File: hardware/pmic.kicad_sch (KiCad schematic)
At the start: 11 parts, among them U501 RK809-5

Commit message: Calculate captured PMIC capacitor bank bias margins
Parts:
- C501, C502, C503, C504, C505, C506, C507, C508: Qualification Effective-capacitance review and load stability pending -> Typical bias curve reviewed; combined-corner aging and loop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

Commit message: Capture PMIC 1.8V buck channel and expand connectivity checks
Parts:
- added C509, C510, C511, C512: 22uF / 25V, Capacitor_SMD:C_1210_3225Metric, symbol Device:C_Small
- added L505: 0.47uH, Inductor_SMD:L_Coilcraft_XxL4020, symbol Device:L_Small
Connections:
- net GND: now also C509.2, C510.2, C511.2, C512.2
- net PMIC_SW5: now reaches U501.53 (SW5)
- net PMIC_SW5: now also L505.1
- net 3V3_MAIN: now reaches U501.54 (VCC9)
- net 3V3_MAIN: now also C512.1
- net VCC_1V8: now reaches U501.59 (FB5)
- net VCC_1V8: now also C509.1, C510.1, C511.1, L505.2
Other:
- note added: "BUCK5: 1.8V startup / 2.5A rated; 3 x 22uF output bank"
- note added: "PMIC capture in progress — BUCK1 / BUCK2 / BUCK5"
- note removed: "PMIC capture in progress — BUCK1 / BUCK2"
- moved on the sheet: U501D

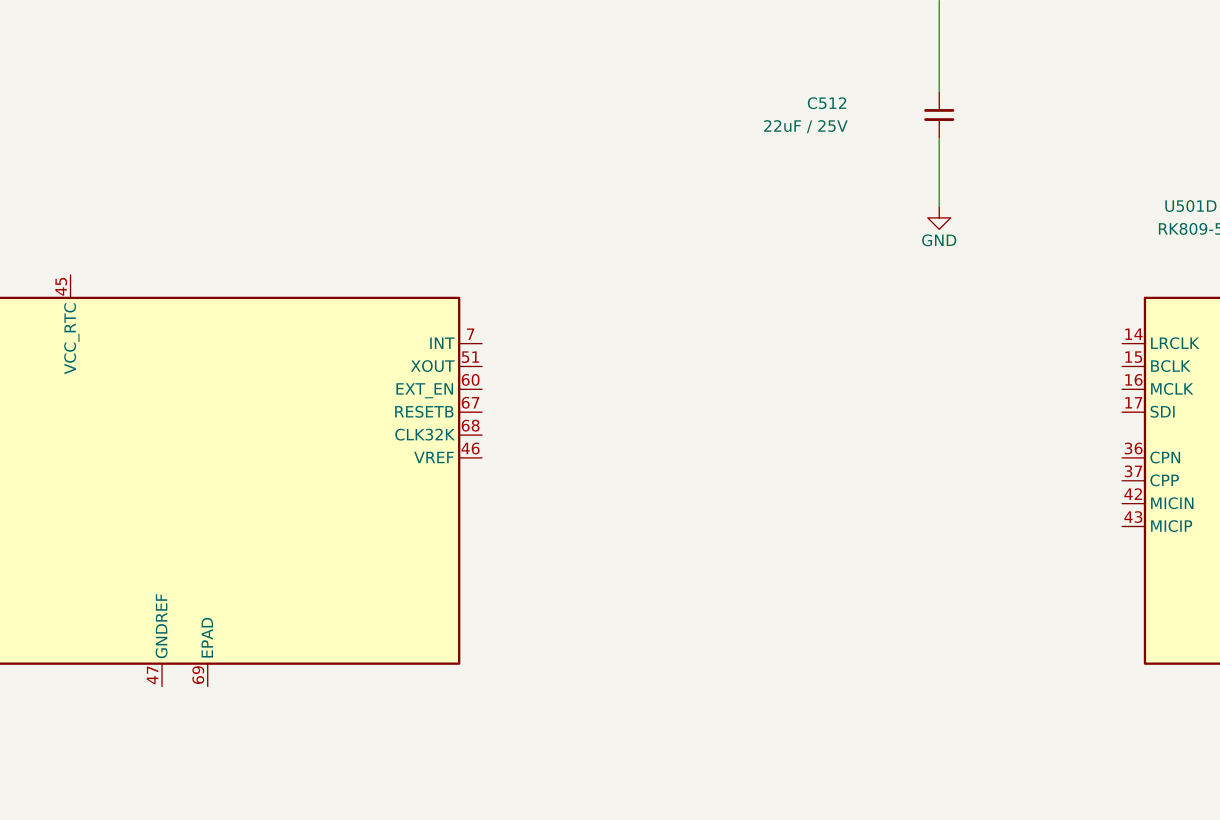
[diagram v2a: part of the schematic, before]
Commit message: Capture PMIC ground return and processor reset network
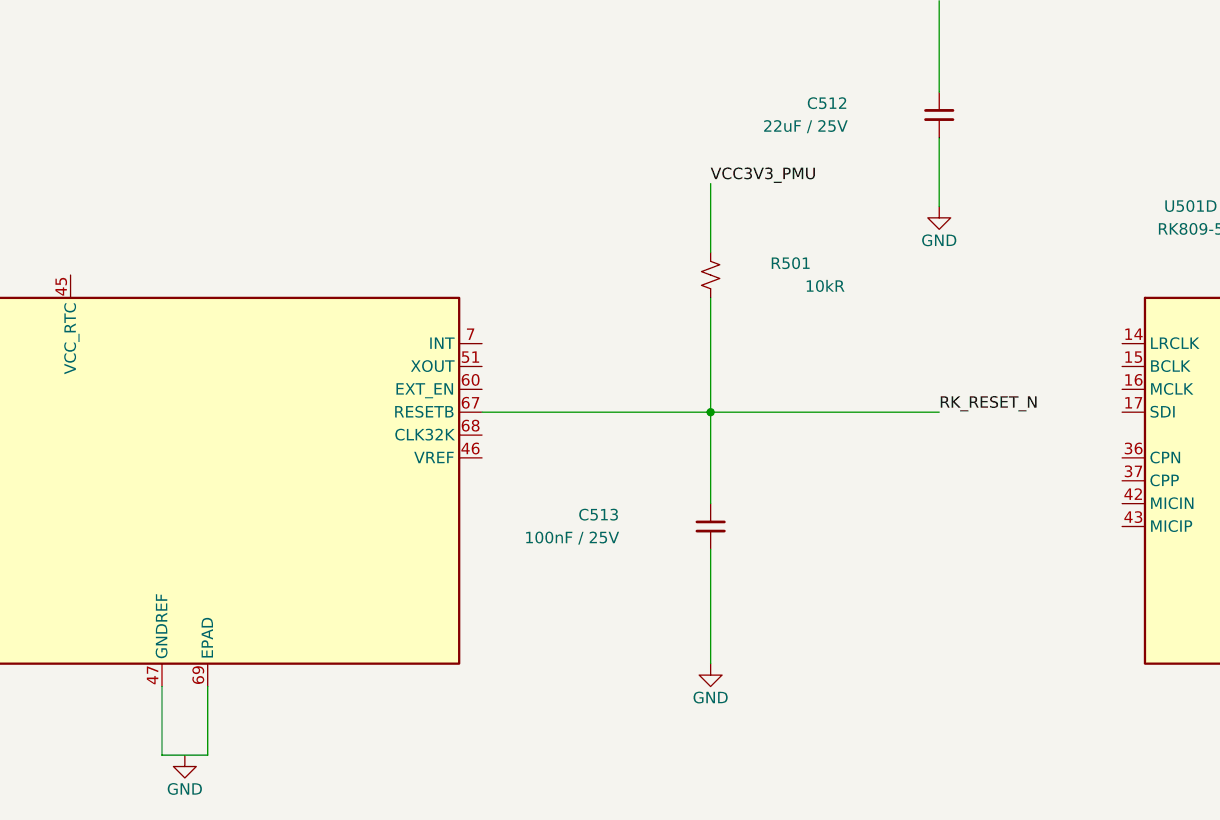
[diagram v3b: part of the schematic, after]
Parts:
- added C513: 100nF / 25V, Capacitor_SMD:C_0603_1608Metric, symbol Device:C_Small
- added R501: 10kR, Resistor_SMD:R_0603_1608Metric, symbol Device:R_Small_US
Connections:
- net GND: now also C513.2
- net at U501.47 (GNDREF): now also U501.69 (EPAD)
- net RK_RESET_N: now reaches U501.67 (RESETB)
- net RK_RESET_N: now also C513.1, R501.2
- new net VCC3V3_PMU: R501.1

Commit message: Capture PMIC RTC and internal-reference bypass circuits
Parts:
- added C514, C515: 1uF / 25V, Capacitor_SMD:C_0603_1608Metric, symbol Device:C_Small
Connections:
- net 3V3_MAIN: now also U501.45 (VCC_RTC), C514.1
- net GND: now also C514.2, C515.2
- net at U501.46 (VREF): now also C515.1

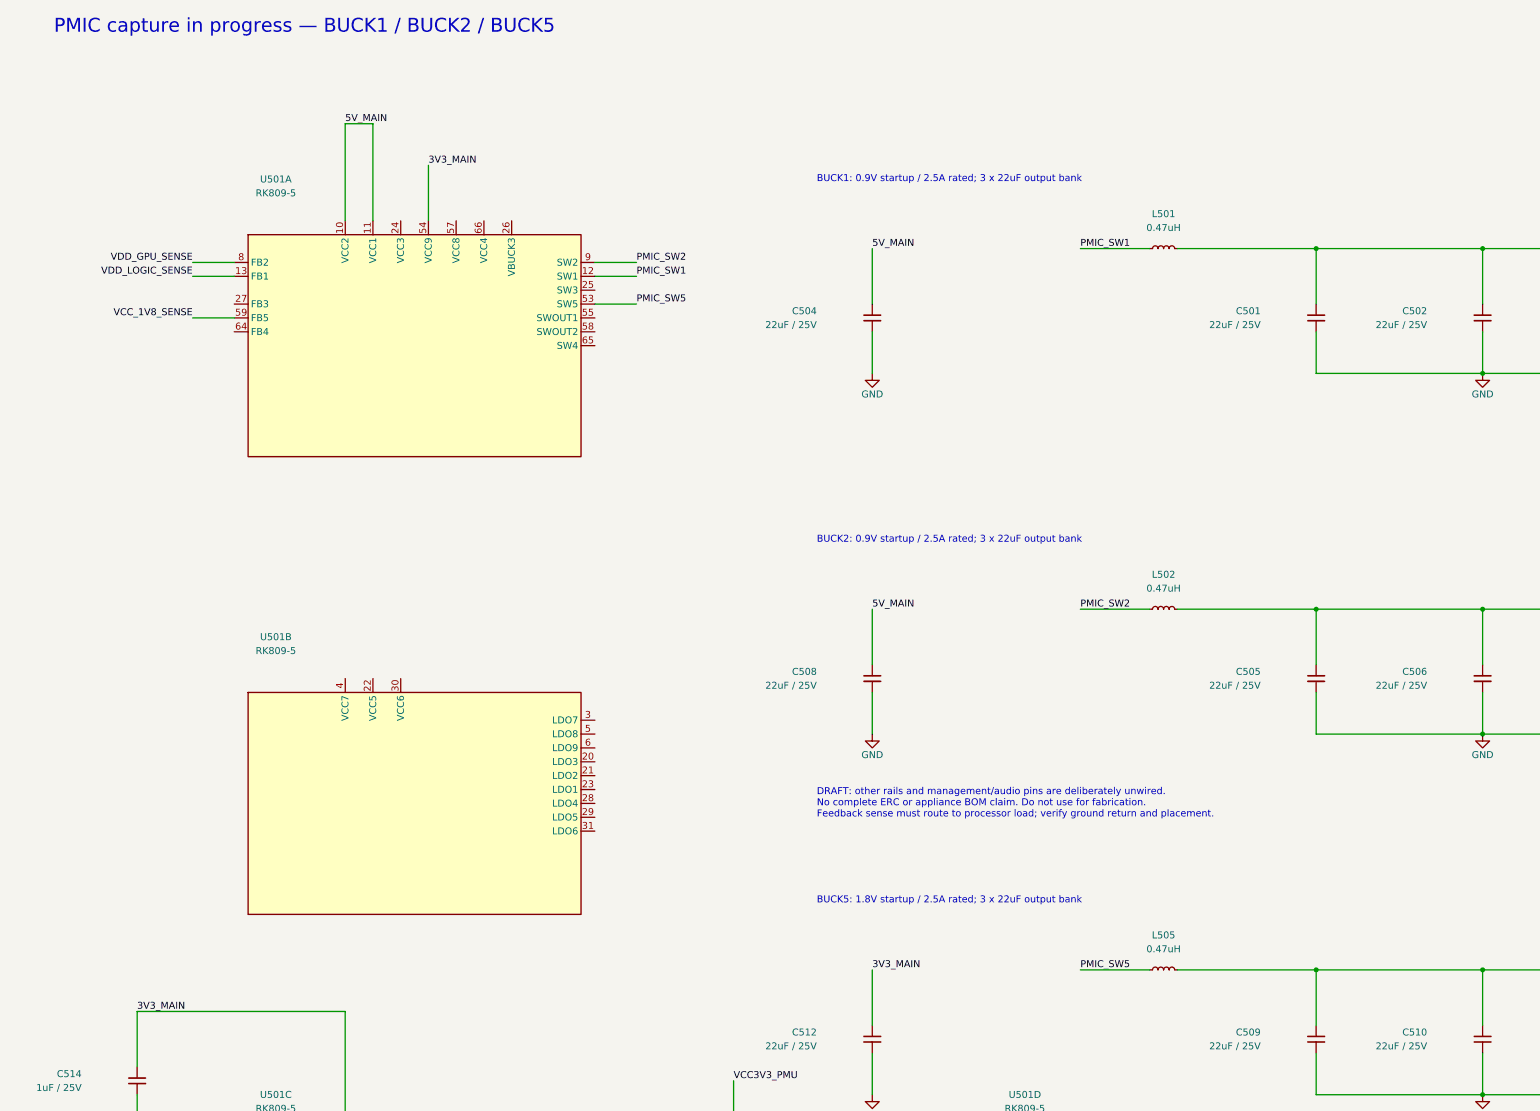
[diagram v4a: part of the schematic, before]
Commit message: Enforce PMIC RTC voltage rule and capture 3.3V PMU LDO
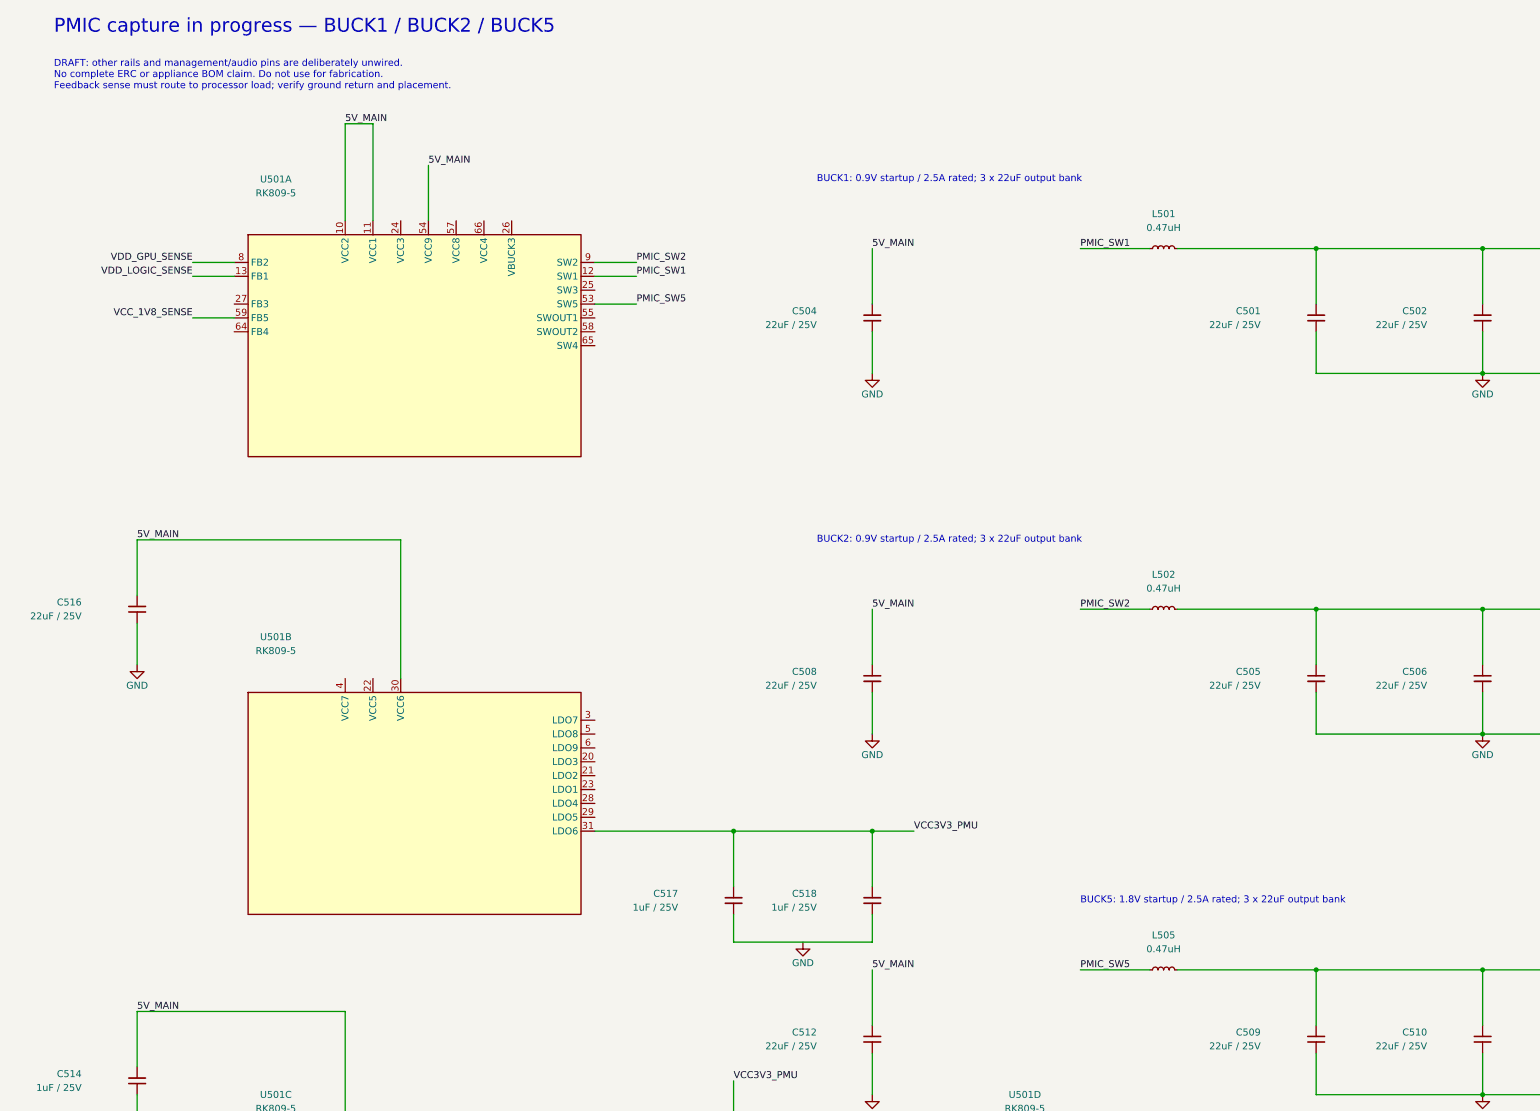
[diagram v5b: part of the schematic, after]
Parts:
- added C516: 22uF / 25V, Capacitor_SMD:C_1210_3225Metric, symbol Device:C_Small
- added C517, C518: 1uF / 25V, Capacitor_SMD:C_0603_1608Metric, symbol Device:C_Small
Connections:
- net 3V3_MAIN is gone; now on net 5V_MAIN: C512.1, C514.1, U501.45 (VCC_RTC), U501.54 (VCC9)
- net 5V_MAIN: now also U501.30 (VCC6), C516.1
- net GND: now also C516.2
- net VCC3V3_PMU: now also U501.31 (LDO6), C517.1, C518.1
- new net: C517.2, C518.2

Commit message: Capture separate processor analog LDO rails
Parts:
- added C519: 22uF / 25V, Capacitor_SMD:C_1210_3225Metric, symbol Device:C_Small
- added C520, C521, C522, C523: 1uF / 25V, Capacitor_SMD:C_0603_1608Metric, symbol Device:C_Small
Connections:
- net GND: now also C519.2
- net VDDA0V9_PMU: now reaches U501.20 (LDO3)
- net VDDA0V9_PMU: now also C522.1, C523.1
- net VDDA_0V9: now reaches U501.21 (LDO2)
- net VDDA_0V9: now also C520.1, C521.1
- net 3V3_MAIN: now reaches U501.22 (VCC5)
- net 3V3_MAIN: now also C519.1
- new net: C522.2, C523.2
- new net: C520.2, C521.2
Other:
- note added: "LDO2: 0.9V / 400mA; load budget pending"
- note added: "LDO3: 0.9V / 100mA high PSRR; load budget pending"

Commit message: Capture enabled analog and SD IO LDO outputs
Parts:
- added C524: 22uF / 25V, Capacitor_SMD:C_1210_3225Metric, symbol Device:C_Small
- added C525, C526, C527, C528, C529, C530: 1uF / 25V, Capacitor_SMD:C_0603_1608Metric, symbol Device:C_Small
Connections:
- net 3V3_MAIN: now also U501.4 (VCC7), C524.1
- net GND: now also C524.2
- net VCCIO_SD: now reaches U501.29 (LDO5)
- net VCCIO_SD: now also C529.1, C530.1
- net VCCA1V8_PMU: now reaches U501.3 (LDO7)
- net VCCA1V8_PMU: now also C525.1, C526.1
- net VCCA_1V8: now reaches U501.5 (LDO8)
- net VCCA_1V8: now also C527.1, C528.1
- new net: C529.2, C530.2
- new net: C525.2, C526.2
- new net: C527.2, C528.2
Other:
- note added: "LDO5: 3.3V startup / slot 4; SD IO adjustable; load budget pending"
- note added: "LDO7: 1.8V / slot 2; load budget pending"
- note added: "LDO8: 1.8V / slot 2; load budget pending"
- note added: "PMIC capture in progress — buck / analog / IO rails"
- note removed: "PMIC capture in progress — BUCK1 / BUCK2 / BUCK5"

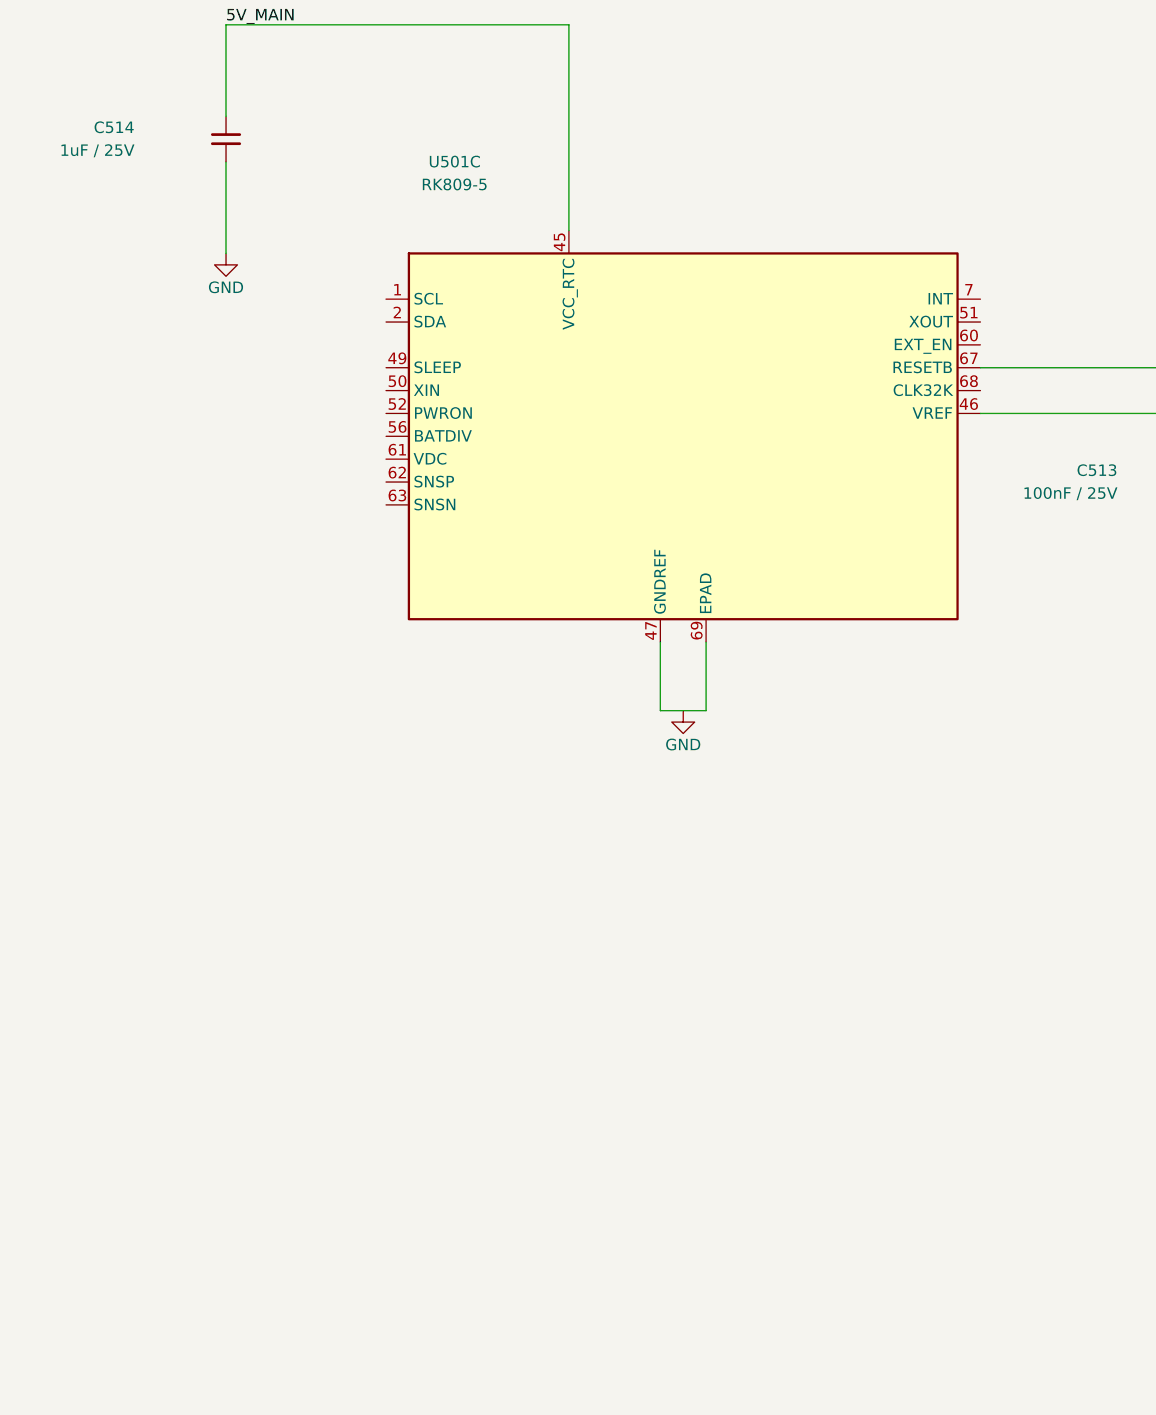
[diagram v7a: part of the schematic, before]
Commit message: Capture PMIC I2C pullups with domain and timing constraints
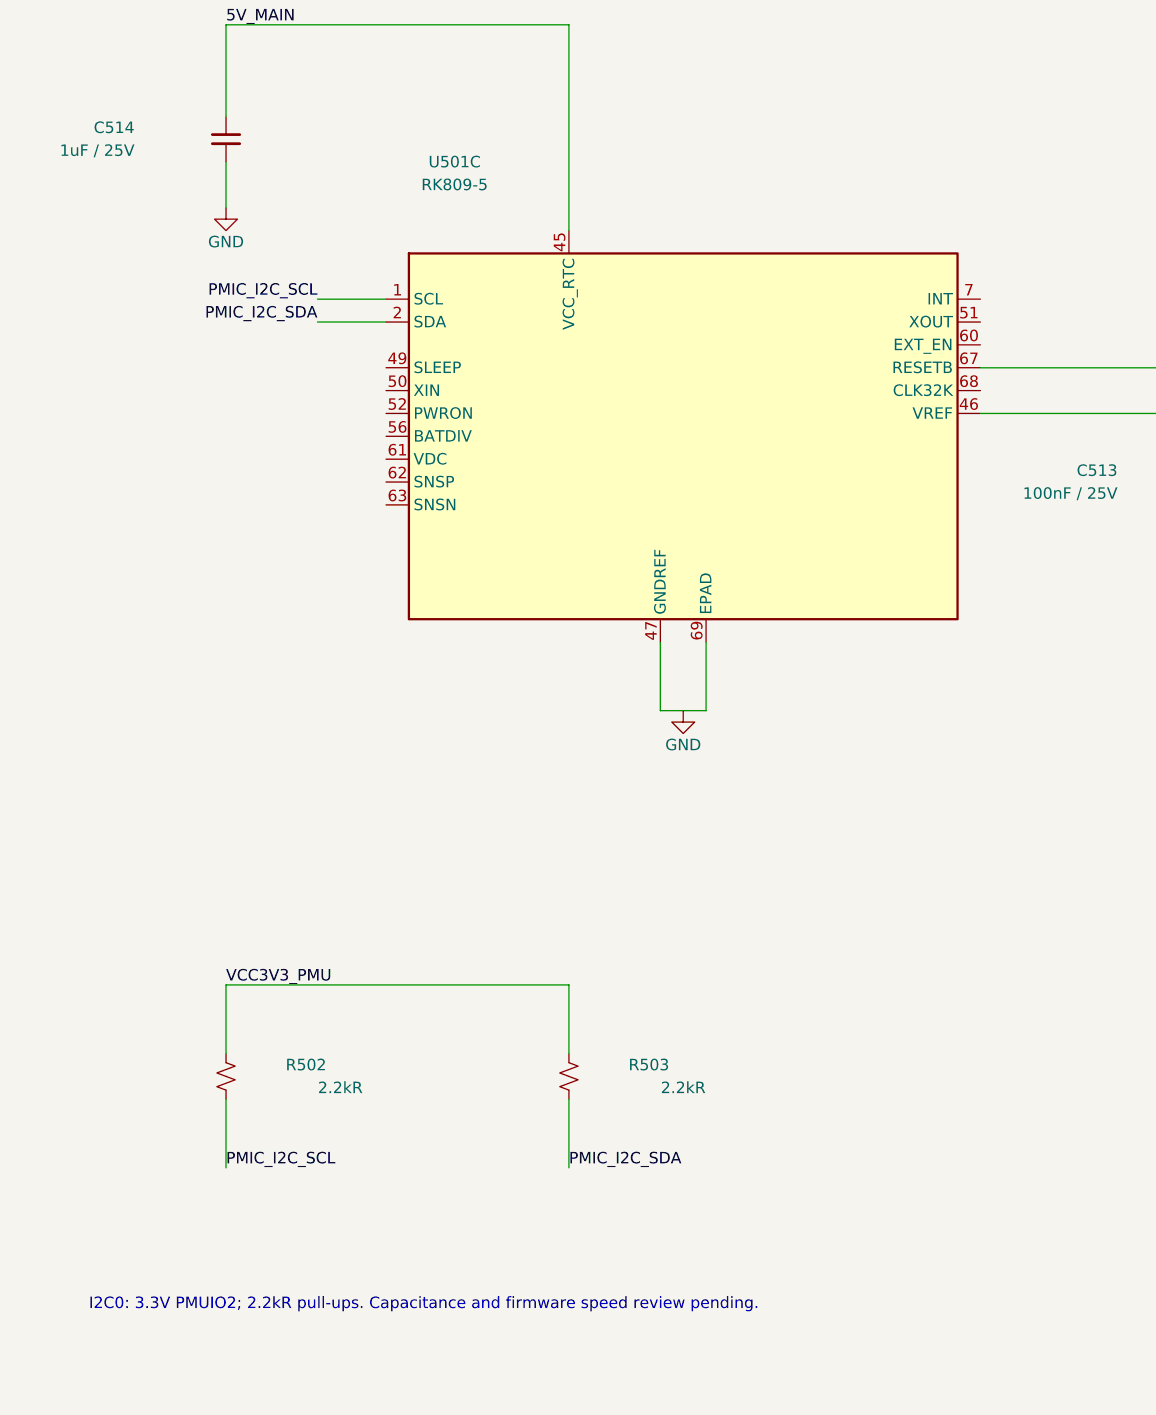
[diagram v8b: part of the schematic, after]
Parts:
- added R502, R503: 2.2kR, Resistor_SMD:R_0603_1608Metric, symbol Device:R_Small_US
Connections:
- net VCC3V3_PMU: now also R502.1, R503.1
- net PMIC_I2C_SCL: now reaches U501.1 (SCL)
- net PMIC_I2C_SCL: now also R502.2
- net PMIC_I2C_SDA: now reaches U501.2 (SDA)
- net PMIC_I2C_SDA: now also R503.2
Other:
- note added: "I2C0: 3.3V PMUIO2; 2.2kR pull-ups. Capacitance and firmware speed review pending."
